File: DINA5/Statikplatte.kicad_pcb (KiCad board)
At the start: 2 copper layers, 210 x 148 mm, 35 parts, among them J1 VIN, J10 HV, J11 SCREW, J12 SCREW, J13 SCREW, J14 SCREW, J2 GND, J3 GND, J4 GND, J5 GND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

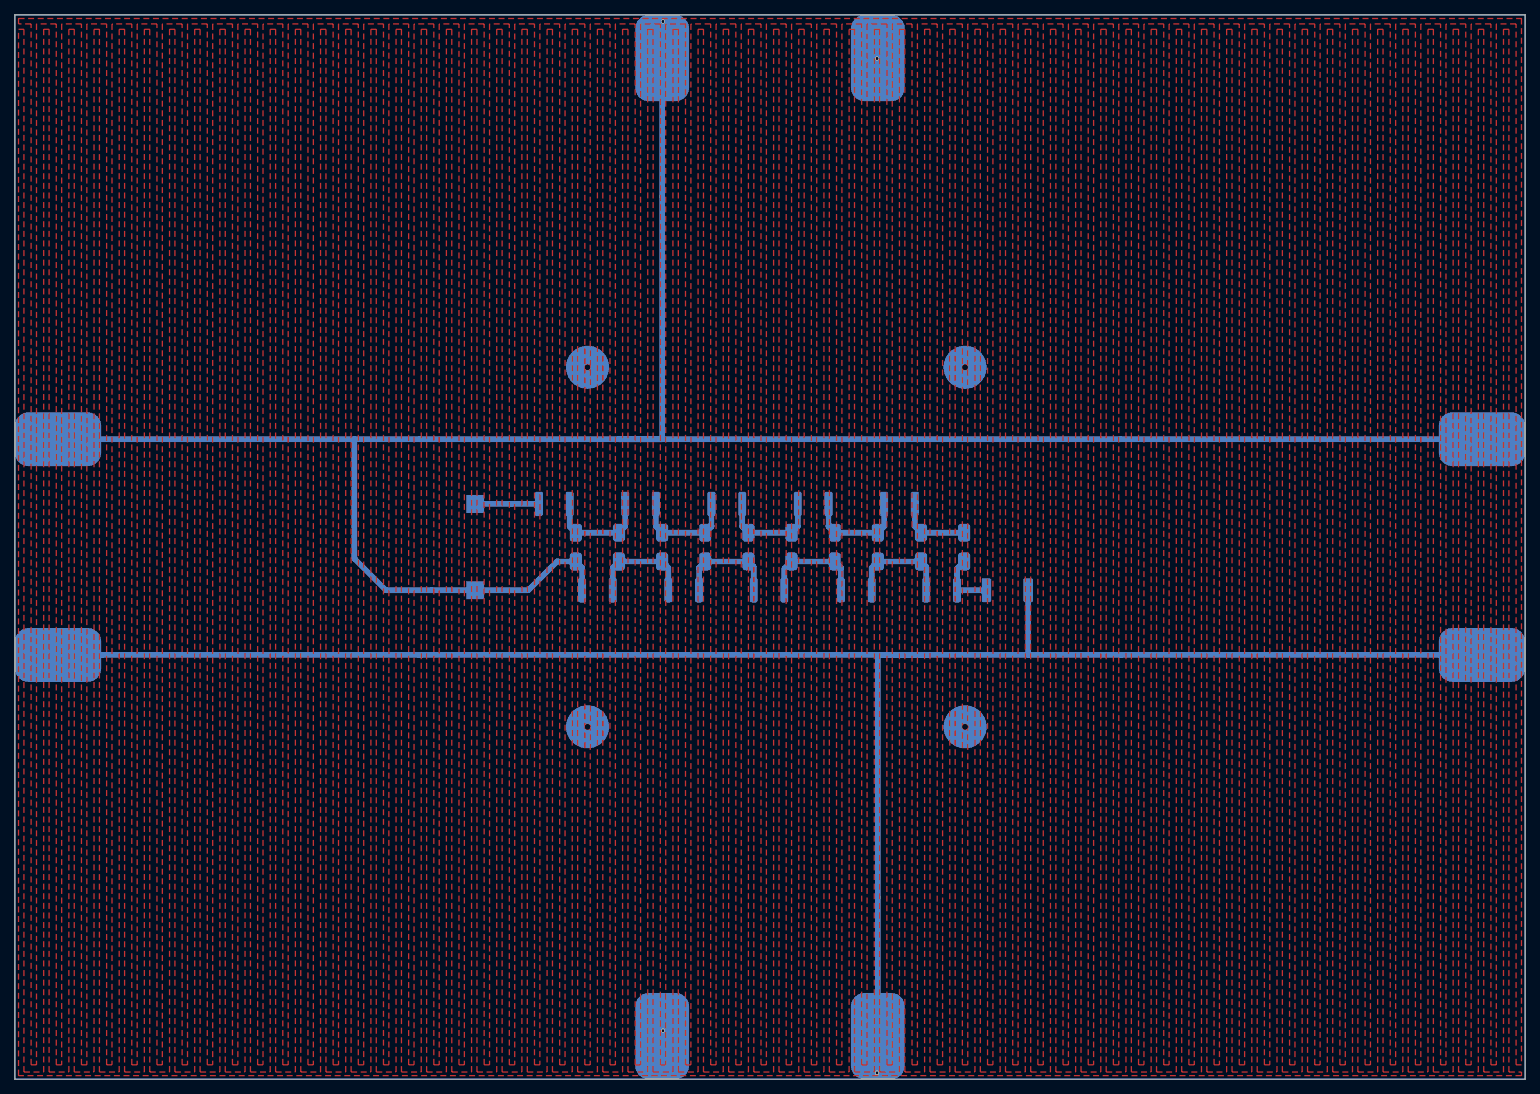
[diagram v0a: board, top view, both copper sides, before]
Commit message: moved screws and added contributor
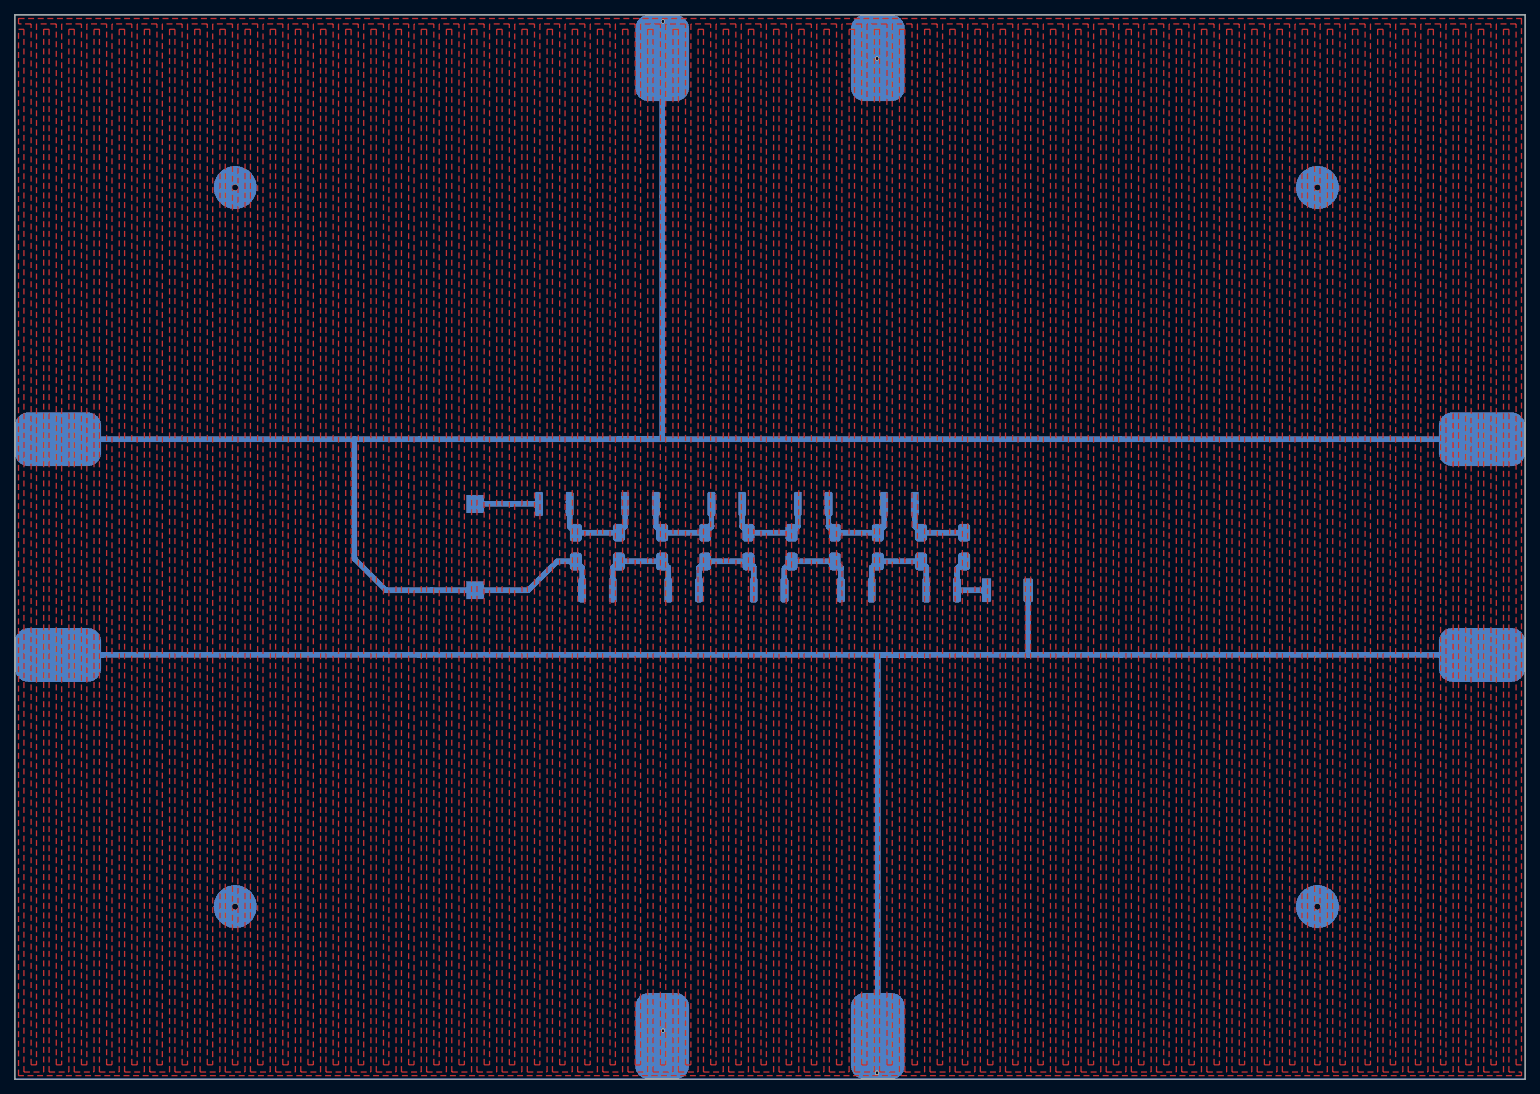
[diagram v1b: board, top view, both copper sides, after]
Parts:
- added G***: LOGO, otter:otterimage, B.Cu at (197.2, 36.5)
- moved J11 55.0 mm to (196.1, 39.0)
- moved J12 55.0 mm to (196.1, 139.0)
- moved J13 55.0 mm to (45.6, 39.0)
- moved J14 55.0 mm to (45.6, 139.0)
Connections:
- J11 pad 2: (no net) -> /GND
- J12 pad 2: (no net) -> /GND
- J14 pad 2: (no net) -> /GND
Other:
- board text added: "Design by Jan Henrik Hemsing and Niklas Fauth"
- board text added: "Electrostatic adhesion plate"
- board text removed: "Electrostatic adhesion plate Design by Jan Henrik Hemsing"

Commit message: added resistor to gnd
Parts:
- added R2: 33M, Resistor_SMD:R_2512_6332Metric, B.Cu at (85.9, 93.0)
- moved G*** 0.07 mm to (197.3, 36.5)
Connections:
- J2 pad 1: /GND -> /GNDE
- J4 pad 1: /GND -> /GNDE
- J5 pad 1: /GND -> /GNDE
- J6 pad 1: /GND -> /GNDE
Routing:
- net /GND: track 312.2 -> 20.0 mm, vias 2 -> 0
- net /GNDE: track 0.00 -> 288.2 mm, vias 0 -> 2
- added copper zone on F.Cu, net /GNDE
- removed copper zone on F.Cu, net /GND
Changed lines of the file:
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@@
     (tracks 84)
     (zones 0)
-    (modules 36)
-    (nets 14)
+    (modules 37)
+    (nets 15)
   )
   (page A4)
@@
   )
   (setup
-    (last_trace_width 0.25)
+    (last_trace_width 0.8)
     (user_trace_width 0.4)
     (user_trace_width 0.6)
@@
   (net 12 /N10)
   (net 13 /HV)
+  (net 14 /GNDE)
   (net_class Default "Dies ist die voreingestellte Netzklasse."
     (clearance 0.2)
@@
     (uvia_drill 0.1)
     (add_net /GND)
+    (add_net /GNDE)
     (add_net /HV)
     (add_net /N1)
@@
     (add_net "Net-(C1-Pad2)")
   )
+  (module Resistor_SMD:R_2512_6332Metric (layer B.Cu)
+    (at 85.9 93.05 270)
+    (descr "Resistor SMD 2512 (6332 Metric), square (rectangular) end terminal, IPC_7351 nominal, (Body size source: http://www.tortai-tech.com/upload/download/2011102023233369053.pdf), generated with kicad-footprint-generator")
+    (tags resistor)
+    (attr smd)
+    (fp_text reference R2 (at 0 2.62 270) (layer B.SilkS)
+      (effects (font (size 1 1) (thickness 0.15)) (justify mirror))
+    )
+    (fp_text value 33M (at 0 -2.62 270) (layer B.Fab)
+      (effects (font (size 1 1) (thickness 0.15)) (justify mirror))
+    )
+    (fp_text user %R (at 0 0 270) (layer B.Fab)
+      (effects (font (size 1 1) (thickness 0.15)) (justify mirror))
+    )
+    (fp_line (start 3.82 -1.92) (end -3.82 -1.92) (layer B.CrtYd) (width 0.05))
+    (fp_line (start 3.82 1.92) (end 3.82 -1.92) (layer B.CrtYd) (width 0.05))
+    (fp_line (start -3.82 1.92) (end 3.82 1.92) (layer B.CrtYd) (width 0.05))
+    (fp_line (start -3.82 -1.92) (end -3.82 1.92) (layer B.CrtYd) (width 0.05))
+    (fp_line (start -2.052064 -1.71) (end 2.052064 -1.71) (layer B.SilkS) (width 0.12))
+    (fp_line (start -2.052064 1.71) (end 2.052064 1.71) (layer B.SilkS) (width 0.12))
+    (fp_line (start 3.15 -1.6) (end -3.15 -1.6) (layer B.Fab) (width 0.1))
+    (fp_line (start 3.15 1.6) (end 3.15 -1.6) (layer B.Fab) (width 0.1))
+    (fp_line (start -3.15 1.6) (end 3.15 1.6) (layer B.Fab) (width 0.1))
+    (fp_line (start -3.15 -1.6) (end -3.15 1.6) (layer B.Fab) (width 0.1))
+    (pad 2 smd roundrect (at 2.9 0 270) (size 1.35 3.35) (layers B.Cu B.Paste B.Mask) (roundrect_rratio 0.185185)
+      (net 11 /GND))
+    (pad 1 smd roundrect (at -2.9 0 270) (size 1.35 3.35) (layers B.Cu B.Paste B.Mask) (roundrect_rratio 0.185185)
+      (net 14 /GNDE))
+    (model ${KISYS3DMOD}/Resistor_SMD.3dshapes/R_2512_6332Metric.wrl
+      (at (xyz 0 0 0))
+      (scale (xyz 1 1 1))
+      (rotate (xyz 0 0 0))
+    )
+  )
   (module otter:SMAF (layer B.Cu)
     (at 93 89 270)
@@
       (effects (font (size 1 1) (thickness 0.15)) (justify mirror))
     )
-    (pad 2 smd circle (at 0 0) (size 6 6) (layers B.Cu B.Paste B.Mask)
-      (net 11 /GND))
-    (pad 2 thru_hole oval (at 0 0) (size 0.9 0.9) (drill 0.8) (layers F.Cu)
-      (net 11 /GND))
+    (pad 1 smd circle (at 0 0) (size 6 6) (layers B.Cu B.Paste B.Mask)
+      (net 14 /GNDE))
+    (pad 1 thru_hole oval (at 0 0) (size 0.9 0.9) (drill 0.8) (layers F.Cu)
+      (net 14 /GNDE))
     (model "/home/janhenrik/Downloads/9774050360R (rev1).stp"
       (offset (xyz 0 0 5))
@@
       (effects (font (size 1 1) (thickness 0.15)) (justify mirror))
     )
-    (pad 2 smd circle (at 0 0) (size 6 6) (layers B.Cu B.Paste B.Mask)
-      (net 11 /GND))
-    (pad 2 thru_hole oval (at 0 0) (size 0.9 0.9) (drill 0.8) (layers F.Cu)
-      (net 11 /GND))
+    (pad 1 smd circle (at 0 0) (size 6 6) (layers B.Cu B.Paste B.Mask)
+      (net 14 /GNDE))
+    (pad 1 thru_hole oval (at 0 0) (size 0.9 0.9) (drill 0.8) (layers F.Cu)
+      (net 14 /GNDE))
     (model "/home/janhenrik/Downloads/9774050360R (rev1).stp"
       (offset (xyz 0 0 5))
@@
       (effects (font (size 1 1) (thickness 0.15)) (justify mirror))
     )
-    (pad 2 smd circle (at 0 0) (size 6 6) (layers B.Cu B.Paste B.Mask)
-      (net 11 /GND))
-    (pad 2 thru_hole oval (at 0 0) (size 0.9 0.9) (drill 0.8) (layers F.Cu)
-      (net 11 /GND))
+    (pad 1 smd circle (at 0 0) (size 6 6) (layers B.Cu B.Paste B.Mask)
+      (net 14 /GNDE))
+    (pad 1 thru_hole oval (at 0 0) (size 0.9 0.9) (drill 0.8) (layers F.Cu)
+      (net 14 /GNDE))
     (model "/home/janhenrik/Downloads/9774050360R (rev1).stp"
       (offset (xyz 0 0 5))
@@
       (effects (font (size 1 1) (thickness 0.15)) (justify mirror))
     )
-    (pad 2 smd circle (at 0 0) (size 6 6) (layers B.Cu B.Paste B.Mask)
-      (net 11 /GND))
-    (pad 2 thru_hole oval (at 0 0) (size 0.9 0.9) (drill 0.8) (layers F.Cu)
-      (net 11 /GND))
+    (pad 1 smd circle (at 0 0) (size 6 6) (layers B.Cu B.Paste B.Mask)
+      (net 14 /GNDE))
+    (pad 1 thru_hole oval (at 0 0) (size 0.9 0.9) (drill 0.8) (layers F.Cu)
+      (net 14 /GNDE))
     (model "/home/janhenrik/Downloads/9774050360R (rev1).stp"
       (offset (xyz 0 0 5))
@@
     )
     (pad 1 smd roundrect (at 0 0 180) (size 12 7.5) (layers B.Cu B.Paste B.Mask) (roundrect_rratio 0.25)
-      (net 11 /GND))
+      (net 14 /GNDE))
   )
   (module otter:PAD7.5x12 (layer B.Cu)
@@
     )
     (pad 1 smd roundrect (at 0 0 270) (size 12 7.5) (layers B.Cu B.Paste B.Mask) (roundrect_rratio 0.25)
-      (net 11 /GND))
+      (net 14 /GNDE))
   )
   (module otter:PAD7.5x12 (layer B.Cu)
@@
     )
     (pad 1 smd roundrect (at 0 0 180) (size 12 7.5) (layers B.Cu B.Paste B.Mask) (roundrect_rratio 0.25)
-      (net 11 /GND))
+      (net 14 /GNDE))
   )
   (module otter:PAD7.5x12 (layer B.Cu)
@@
     )
     (pad 1 smd roundrect (at 0 0 270) (size 12 7.5) (layers B.Cu B.Paste B.Mask) (roundrect_rratio 0.25)
-      (net 11 /GND))
+      (net 14 /GNDE))
   )
   (module TestPoint:TestPoint_Pad_2.5x2.5mm (layer B.Cu)
@@
   )
   (module otter:otterimage (layer B.Cu)
-    (at 197.19 36.53 315)
+    (at 197.26 36.54 315)
     (fp_text reference G*** (at 0 0 315) (layer B.SilkS) hide
       (effects (font (size 1.524 1.524) (thickness 0.3)) (justify mirror))
@@
   (segment (start 93.000001 86.999999) (end 93 87) (width 0.8) (layer B.Cu) (net 10))
   (segment (start 99 86.999999) (end 93.000001 86.999999) (width 0.8) (layer B.Cu) (net 10))
-  (via (at 105.11 15.91) (size 0.6) (drill 0.4) (layers F.Cu B.Cu) (net 11))
-  (via (at 105.12 156.25) (size 0.6) (drill 0.4) (layers F.Cu B.Cu) (net 11))
+  (via (at 105.11 15.91) (size 0.6) (drill 0.4) (layers F.Cu B.Cu) (net 14))
+  (via (at 105.12 156.25) (size 0.6) (drill 0.4) (layers F.Cu B.Cu) (net 14))
   (segment (start 93.8625 91.8625) (end 93 91) (width 0.8) (layer B.Cu) (net 11))
   (segment (start 93.8625 95) (end 93.8625 91.8625) (width 0.8) (layer B.Cu) (net 11))
-  (segment (start 71.25 74) (end 99 74) (width 0.8) (layer B.Cu) (net 11))
-  (segment (start 99 74) (end 168.75 74) (width 0.8) (layer B.Cu) (net 11))
-  (segment (start 71.25 74) (end 21 74) (width 0.8) (layer B.Cu) (net 11))
-  (segment (start 168.75 74) (end 219 74) (width 0.8) (layer B.Cu) (net 11))
-  (segment (start 105 74) (end 99 74) (width 0.8) (layer B.Cu) (net 11))
-  (segment (start 105 40.25) (end 105 74) (width 0.8) (layer B.Cu) (net 11))
-  (segment (start 90.4 91) (end 93 91) (width 0.8) (layer B.Cu) (net 11))
-  (segment (start 79 95) (end 86.4 95) (width 0.8) (layer B.Cu) (net 11))
-  (segment (start 86.4 95) (end 90.4 91) (width 0.8) (layer B.Cu) (net 11))
-  (segment (start 79 95) (end 72.9 95) (width 0.8) (layer B.Cu) (net 11))
-  (segment (start 72.9 95) (end 66.6 95) (width 0.8) (layer B.Cu) (net 11))
-  (segment (start 66.6 95) (end 62.2 90.6) (width 0.8) (layer B.Cu) (net 11))
-  (segment (start 62.2 90.6) (end 62.2 74) (width 0.8) (layer B.Cu) (net 11))
-  (segment (start 105 40.25) (end 105 21) (width 0.8) (layer B.Cu) (net 11))
+  (segment (start 79.95 95.95) (end 79 95) (width 0.8) (layer B.Cu) (net 11))
+  (segment (start 85.9 95.95) (end 79.95 95.95) (width 0.8) (layer B.Cu) (net 11))
+  (segment (start 92.9125 95.95) (end 93.8625 95) (width 0.8) (layer B.Cu) (net 11))
+  (segment (start 85.9 95.95) (end 92.9125 95.95) (width 0.8) (layer B.Cu) (net 11))
+  (segment (start 71.25 74) (end 99 74) (width 0.8) (layer B.Cu) (net 14))
+  (segment (start 99 74) (end 168.75 74) (width 0.8) (layer B.Cu) (net 14))
+  (segment (start 71.25 74) (end 21 74) (width 0.8) (layer B.Cu) (net 14))
+  (segment (start 168.75 74) (end 219 74) (width 0.8) (layer B.Cu) (net 14))
+  (segment (start 105 74) (end 99 74) (width 0.8) (layer B.Cu) (net 14))
+  (segment (start 105 40.25) (end 105 74) (width 0.8) (layer B.Cu) (net 14))
+  (segment (start 105 40.25) (end 105 21) (width 0.8) (layer B.Cu) (net 14))
   (segment (start 146 92) (end 147 91) (width 0.8) (layer B.Cu) (net 12))
   (segment (start 146 95) (end 146 92) (width 0.8) (layer B.Cu) (net 12))
@@
   (segment (start 155.9 103.9) (end 155.9 95) (width 0.8) (layer B.Cu) (net 13))
   (segment (start 156 104) (end 168.75 104) (width 0.8) (layer B.Cu) (net 13))
-  (zone (net 11) (net_name /GND) (layer F.Cu) (hatch edge 0.508)
+  (segment (start 85.9 90.15) (end 73 90.15) (width 0.8) (layer B.Cu) (net 14))
+  (segment (start 73 90.15) (end 67.85 85) (width 0.8) (layer B.Cu) (net 14))
+  (segment (start 67.85 85) (end 67.85 74) (width 0.8) (layer B.Cu) (net 14))
+  (zone (net 14) (net_name /GNDE) (layer F.Cu) (hatch edge 0.508)
     (priority 4)
     (connect_pads yes (clearance 0))
